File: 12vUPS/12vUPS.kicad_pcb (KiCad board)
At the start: 2 copper layers, 65.4 x 60.8 mm, 18 parts, among them J1 INPUT, J2 BATTERY, J3 OUTPUT, J4 ENABLE, K1 VEGHA L08A0212VDC, Q1 BDX53C

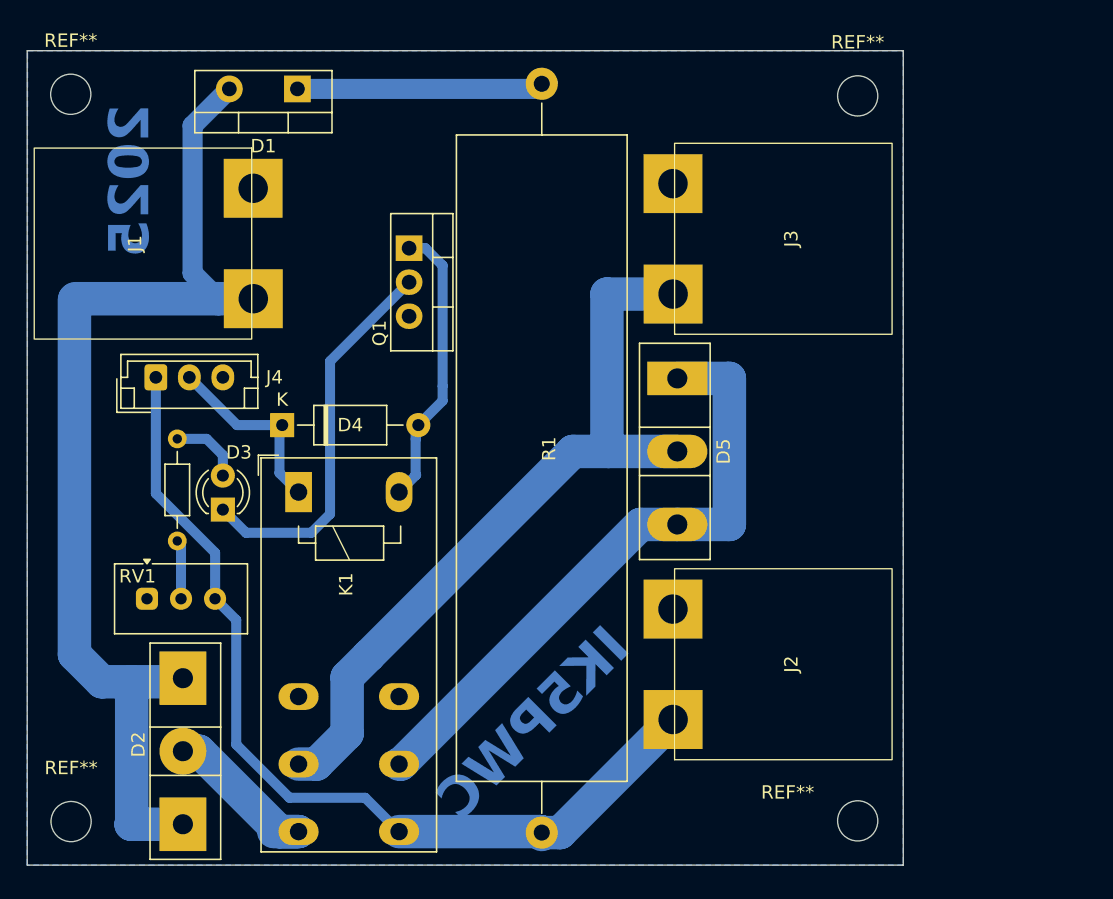
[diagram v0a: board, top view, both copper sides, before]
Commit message: Update 12vUPS-2025-06-08_110639.zip, 12vUPS-2025-06-08_231957.zip, 12vUPS-2025-06-08_232518.zip, and 11 more files
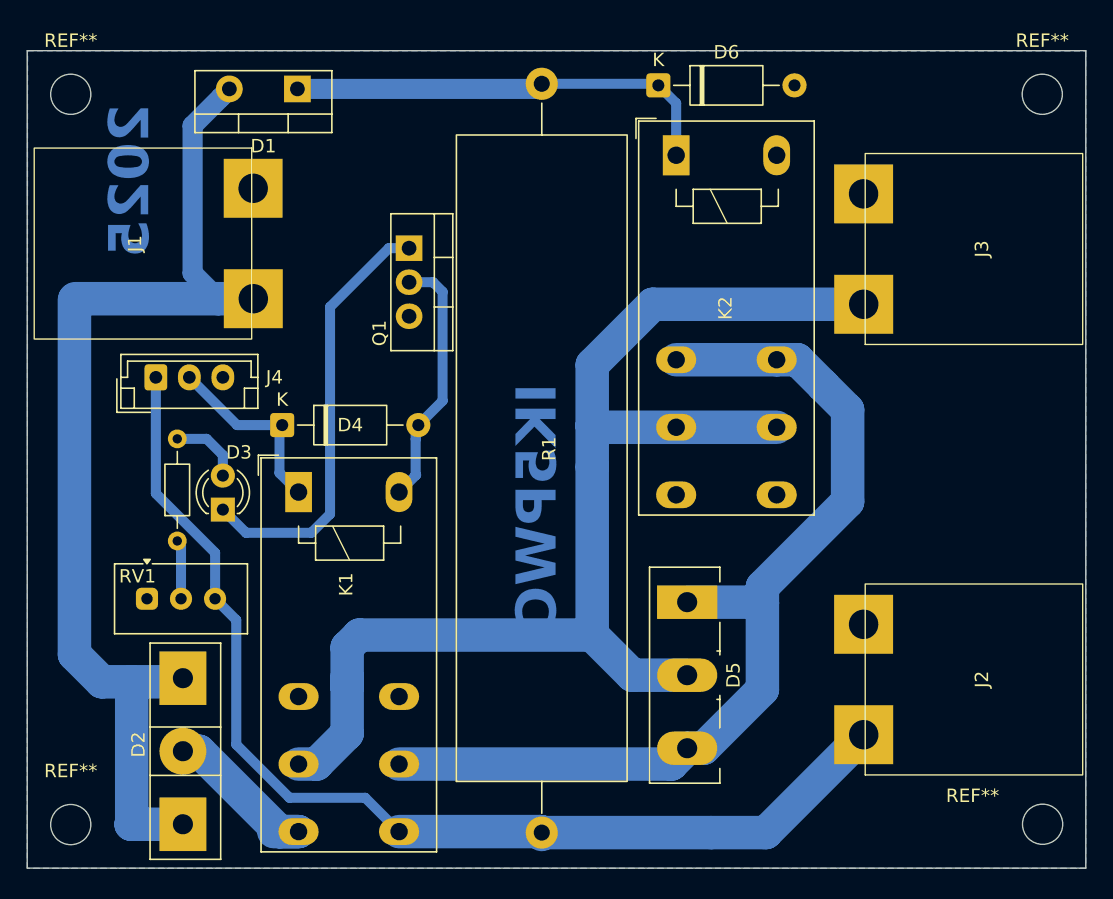
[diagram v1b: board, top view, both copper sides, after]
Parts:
- added D6: 1N4001, Diode_THT:D_A-405_P10.16mm_Horizontal, F.Cu at (59.9, 19.0)
- added K2: VEGHA L08A0212VDC, IK5PWC:VEGhA L08 12V dc, F.Cu at (61.2, 24.2)
- moved D5 16.7 mm to (62.0, 57.5)
- moved J2 14.3 mm to (75.2, 67.4)
- moved J3 14.2 mm to (75.2, 35.3)
- moved REF** 13.8 mm to (88.6, 74.1)
- moved REF** 13.8 mm to (88.5, 19.6)
- moved REF** 0.23 mm to (16.0, 74.1)
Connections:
- net /A1 renamed /ENA
- net Net-(D1-K) renamed /X1
- D4 pad 2: /A2 -> Net-(D4-A)
- K1 pad A2: /A2 -> Net-(D4-A)
- Q1 pad 1: /A2 -> Net-(D3-K)
- Q1 pad 2: Net-(D3-K) -> Net-(D4-A)
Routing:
- net Net-(D5-K): track 57.1 -> 94.8 mm
- net Net-(D5-A-Pad1): track 46.8 -> 72.9 mm
- net /A2: track 21.5 -> 0.00 mm
- net Net-(D4-A): track 0.00 -> 19.3 mm
- net /X1: track 19.1 -> 33.6 mm
- net /+12V: track 69.0 -> 82.8 mm
- net Net-(D3-K): track 29.0 -> 32.5 mm
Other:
- board size 65.4 x 60.8 mm -> 79 x 61 mm

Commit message: Update 12vUPS-2025-06-10_185612.zip, 12vUPS-2025-06-10_190121.zip, 12vUPS-2025-06-10_190645.zip, and 3 more files
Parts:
- removed D5: D_Schottky_Dual_CommonCathode_AKA_Parallel, Package_TO_SOT_THT:TO-247-3_Vertical
- removed K2: VEGHA L08A0212VDC, IK5PWC:VEGhA L08 12V dc
- D6: value 1N4001 -> W01G; footprint Diode_THT:D_A-405_P10.16mm_Horizontal -> Diode_THT:Diode_Bridge_Round_D9.8mm
- moved D6 24.9 mm to (35.5, 24.3)
- moved R2 7.55 mm to (24.0, 45.4), turned to -90 degrees
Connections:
- D1 pad 1: /X1 -> Net-(D1-K)
- D1 pad 2: VCC -> /INPUT
- D2 pad 2: VCC -> /INPUT
- D6 pad 1: /X1 -> Net-(D6-+)
- D6 pad 2: GND -> /OUT
- J1 pad 2: VCC -> /INPUT
- J2 pad 1: /+12V -> /BATT
- J3 pad 1: Net-(D5-K) -> /OUT
- J4 pad 1: /+12V -> /BATT
- K1 pad 11: Net-(D5-K) -> /OUT
- K1 pad 24: /+12V -> /BATT
- R1 pad 1: /+12V -> /BATT
- R1 pad 2: /X1 -> Net-(D1-K)
- R2 pad 1: Net-(R2-Pad1) -> Net-(D3-A)
- R2 pad 2: Net-(D3-A) -> Net-(R2-Pad2)
- RV1 pad 2: Net-(R2-Pad1) -> Net-(R2-Pad2)
- RV1 pad 3: /+12V -> Net-(D6-+)
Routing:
- net Net-(D5-K): track 94.8 -> 0.00 mm
- net /OUT: track 0.00 -> 85.1 mm
- net /+12V: track 82.8 -> 0.00 mm
- net VCC: track 78.2 -> 0.00 mm
- net /INPUT: track 0.00 -> 78.2 mm
- net Net-(D7-A): track 72.9 -> 0.00 mm
- net /BATT: track 0.00 -> 60.5 mm
- net /X1: track 33.6 -> 0.00 mm
- net Net-(D2-K): track 13.0 -> 45.5 mm
- net Net-(D1-K): track 0.00 -> 19.1 mm
- net Net-(R2-Pad2): track 0.00 -> 4.43 mm
- net Net-(R2-Pad1): track 4.43 -> 0.00 mm

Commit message: Update #auto_saved_files#, 12vUPS-2025-06-02_175555.zip, 12vUPS-2025-06-02_180136.zip, and 18 more files
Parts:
- removed D2: 30CPF04, IK5PWC:30CPF04
- removed D6: W01G, Diode_THT:Diode_Bridge_Round_D9.8mm
- added D7: D_Ideal, IK5PWC:D_IDEAL_with_GND, F.Cu at (76.3, 58.9)
- D1: value BYW19 -> SF30GG; footprint Package_TO_SOT_THT:TO-220-2_Vertical -> Diode_THT:D_DO-201AD_P15.24mm_Horizontal
- D3: value LED_Small -> 60CPQ150; footprint LED_THT:LED_D3.0mm -> Package_TO_SOT_THT:TO-247-3_Vertical
- moved D1 29.1 mm to (62.1, 20.0), turned to -90 degrees
- moved D3 23.6 mm to (25.0, 74.1)
- moved REF** 20.1 mm to (68.4, 74.1)
- moved REF** 20.1 mm to (68.4, 19.6)
- moved R2 8.08 mm to (28.3, 52.3), turned to 180 degrees
- moved J2 6.59 mm to (75.1, 74.0)
- moved J4 2.76 mm to (21.5, 43.4)
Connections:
- D1 pad 2: /INPUT -> /OUT
- D3 pad 1: Net-(D3-K) -> /DC_IN
- D3 pad 2: Net-(D3-A) -> /DC-IN-RELE
- D4 pad 2: Net-(D4-A) -> /BJT-GND
- J1 pad 2: /INPUT -> /DC_IN
- J2 pad 1: /BATT -> /BATT_IN
- J4 pad 1: /BATT -> /DC-IN-RELE
- J4 pad 3: GND -> /BJT-GND
- K1 pad 14: Net-(D2-K) -> /DC-IN-RELE
- K1 pad 21: Net-(D7-A) -> /OUT
- K1 pad 24: /BATT -> /DC-IN-RELE
- K1 pad A2: Net-(D4-A) -> /BJT-GND
- Q1 pad 1: Net-(D3-K) -> Net-(Q1-B)
- Q1 pad 2: Net-(D4-A) -> /BJT-GND
- R1 pad 1: /BATT -> /BATT_IN
- R2 pad 1: Net-(D3-A) -> Net-(Q1-B)
- RV1 pad 3: Net-(D6-+) -> /DC-IN-RELE
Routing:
- net /DC-IN-RELE: track 0.00 -> 80.4 mm
- net /INPUT: track 78.2 -> 0.00 mm
- net /BATT_IN: track 0.00 -> 62.0 mm
- net /DC_IN: track 0.00 -> 61.8 mm
- net /BATT: track 60.5 -> 0.00 mm
- net Net-(D2-K): track 45.5 -> 0.00 mm
- net Net-(Q1-B): track 0.00 -> 37.7 mm
- net /BJT-GND: track 0.00 -> 37.5 mm
- net Net-(D3-K): track 32.5 -> 0.00 mm
- net Net-(D4-A): track 19.3 -> 0.00 mm
- net /OUT: track 85.1 -> 67.6 mm
- net Net-(D1-K): track 19.1 -> 12.2 mm
- net Net-(D3-A): track 5.43 -> 0.00 mm
- net Net-(R2-Pad2): track 4.43 -> 5.75 mm
- net /ENA: track 14.0 -> 14.5 mm

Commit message: Update 12vUPS-2025-06-06_224542.zip, 12vUPS-2025-06-06_225111.zip, 12vUPS-2025-06-06_225614.zip, and 28 more files
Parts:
- removed R2: 510, Resistor_THT:R_Axial_DIN0204_L3.6mm_D1.6mm_P7.62mm_Horizontal
- added D5: D, Diode_THT:D_DO-41_SOD81_P10.16mm_Horizontal, F.Cu at (18.2, 59.9)
- added D6: 4V1, Diode_THT:D_DO-35_SOD27_P7.62mm_Horizontal, F.Cu at (20.7, 50.2)
- J4: footprint Connector_JST:JST_EH_B3B-EH-A_1x03_P2.50mm_Vertical -> Connector_JST:JST_EH_B4B-EH-A_1x04_P2.50mm_Vertical
- Q1: value BDX53C -> BC337; footprint Package_TO_SOT_THT:TO-220-3_Vertical -> Package_TO_SOT_THT:TO-92_Inline_Wide
- moved Q1 7.84 mm to (41.9, 38.9), turned to 90 degrees
- moved D3 6.76 mm to (26.7, 67.5), turned to 180 degrees
- moved D4 4.58 mm to (36.4, 44.6), turned to 90 degrees
- moved RV1 2.47 mm to (21.8, 54.8)
- moved J4 2.23 mm to (23.2, 41.9)
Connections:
- D7 pad 1: /DC-IN-RELE -> Net-(D7-K)
- J4 pad 2: /ENA -> Net-(D7-K)
- J4 pad 3: /BJT-GND -> /ENA
- K1 pad 24: /DC-IN-RELE -> Net-(D7-K)
- Q1 pad 1: Net-(Q1-B) -> /BJT-GND
- Q1 pad 2: /BJT-GND -> Net-(D6-A)
- RV1 pad 3: /DC-IN-RELE -> Net-(D5-K)
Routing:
- net Net-(D7-K): track 0.00 -> 72.7 mm
- net Net-(Q1-B): track 37.7 -> 0.00 mm
- net Net-(D6-A): track 0.00 -> 33.1 mm
- net /DC-IN-RELE: track 80.4 -> 52.7 mm
- net Net-(D5-K): track 0.00 -> 12.0 mm
- net /BATT_IN: track 62.0 -> 53.8 mm
- net /BJT-GND: track 37.5 -> 29.8 mm
- net /DC_IN: track 61.8 -> 59.8 mm
- net /ENA: track 14.5 -> 16.5 mm
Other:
- board text added: "DC UPS"

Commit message: Update 12vUPS-2025-06-08_233608.zip, 12vUPS-2025-06-08_234122.zip, 12vUPS-2025-06-22_122202.zip, and 5 more files
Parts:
- D7: footprint IK5PWC:D_IDEAL_with_GND -> IK5PWC:D_IDEAL_no_GND
- moved D7 11.4 mm to (70.2, 49.3), turned to 0 degrees
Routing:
- net Net-(D7-K): track 72.7 -> 79.1 mm
- net /BATT_IN: track 53.8 -> 58.3 mm
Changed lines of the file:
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@@
 		)
 	)
-	(footprint "IK5PWC:D_IDEAL_with_GND"
+	(footprint "IK5PWC:D_IDEAL_no_GND"
 		(layer "F.Cu")
-		(at 76.2975 58.9325 180)
+		(at 70.2175 49.2525)
 		(descr "terminal block Metz Connect Type703_RT10N02HGLU, 2 pins, pitch 9.52mm, size 19x12.5mm^2, drill diamater 1.3mm, pad diameter 2.6mm, see http://www.metz-connect.com/de/system/files/productfiles/Datenblatt_317031_RT10NxxHGLU_OFF-022897S.pdf, script-generated using https://github.com/pointhi/kicad-footprint-generator/scripts/TerminalBlock_MetzConnect")
 		(tags "THT terminal block Metz Connect Type703_RT10N02HGLU pitch 9.52mm size 19x12.5mm^2 drill 1.3mm pad 2.6mm")
@@
 		)
 		(property "Value" "D_Ideal"
-			(at 5.3 -0.23 0)
+			(at -1.4775 -1.935 0)
 			(layer "F.Fab")
 			(effects
@@
 		)
 		(property "Datasheet" ""
-			(at 4.32 25.08 180)
+			(at 4.32 25.08 0)
 			(unlocked yes)
 			(layer "F.Fab")
@@
 		)
 		(property "Description" "Diode"
-			(at 4.32 25.08 180)
+			(at 4.32 25.08 0)
 			(unlocked yes)
 			(layer "F.Fab")
@@
 		)
 		(property "Sim.Device" "D"
-			(at 0 0 180)
+			(at 0 0 0)
 			(unlocked yes)
 			(layer "F.Fab")
@@
 		)
 		(property "Sim.Pins" "1=K 2=A 3=GND"
-			(at 0 0 180)
+			(at 0 0 0)
 			(unlocked yes)
 			(layer "F.Fab")
@@
 		(attr through_hole)
 		(fp_line
-			(start 6.26 -0.615)
-			(end 6.26 9.275)
-			(stroke
-				(width 0.5)
-				(type solid)
-			)
-			(layer "F.SilkS")
-		)
-		(fp_line
-			(start 1.315 4.33)
-			(end 11.205 4.33)
+			(start -3.91 1.77)
+			(end 1.06 1.77)
 			(stroke
 				(width 0.5)
@@
 		)
 		(fp_line
-			(start 1 4.33)
-			(end 5.97 4.33)
-			(stroke
-				(width 0.1)
-				(type default)
-			)
-			(layer "F.SilkS")
-		)
-		(fp_line
-			(start -2.595 4.33)
-			(end 7.295 4.33)
+			(start -0.195 -0.18)
+			(end -0.18 3.83)
 			(stroke
 				(width 0.5)
@@
 		)
 		(fp_rect
-			(start -9.87 11.75)
-			(end 18.12 19.65)
-			(stroke
-				(width 0.1)
-				(type default)
-			)
-			(fill no)
-			(layer "F.SilkS")
-		)
-		(fp_rect
-			(start -9.88 -3.15)
-			(end 18.12 19.65)
-			(stroke
-				(width 0.1)
-				(type solid)
-			)
-			(fill no)
-			(layer "F.SilkS")
-		)
-		(fp_rect
 			(start -9.88 -3.15)
-			(end 18.11 10.79)
+			(end 7.12 6.85)
 			(stroke
 				(width 0.1)
@@
 		(fp_poly
 			(pts
-				(xy 1 -0.615) (xy 1 9.275) (xy 1.025 9.275) (xy 5.97 4.33) (xy 1.025 -0.615)
+				(xy -2.68 -0.225) (xy -2.68 3.855) (xy -0.195 1.77)
 			)
 			(stroke
@@
 		(fp_rect
 			(start -9.98 -3.25)
-			(end 18.22 19.75)
+			(end 7.22 6.95)
 			(stroke
 				(width 0.1)
@@
 			(layer "F.CrtYd")
 		)
-		(fp_line
-			(start 18.11 17.65)
-			(end -9.88 17.65)
-			(stroke
-				(width 0.1)
-				(type solid)
-			)
-			(layer "User.9")
-		)
 		(fp_text user "${REFERENCE}"
-			(at 4.13 17.46 0)
+			(at -0.95 8.42 0)
 			(layer "F.Fab")
 			(effects
@@
 			)
 		)
-		(pad "1" thru_hole circle
-			(at 14.34 4.3 180)
-			(size 5.5 5.5)
-			(drill 2.3)
+		(pad "1" thru_hole rect
+			(at -8.07 5.05)
+			(size 3.5 3.5)
+			(drill 2)
 			(layers "*.Cu" "*.Mask")
 			(remove_unused_layers no)
@@
 			(pintype "passive")
 		)
-		(pad "2" thru_hole circle
-			(at -6.2 4.3 180)
-			(size 5.5 5.5)
-			(drill 2.3)
+		(pad "1" thru_hole rect
+			(at -8.06 -1.34)
+			(size 3.5 3.5)
+			(drill 2)
 			(layers "*.Cu" "*.Mask")
 			(remove_unused_layers no)
-			(net 9 "/BATT_IN")
-			(pinfunction "A")
+			(net 11 "Net-(D7-K)")
+			(pinfunction "K")
 			(pintype "passive")
 		)
-		(pad "3" thru_hole circle
-			(at -6.2 15.01 180)
-			(size 5.5 5.5)
-			(drill 2.3)
+		(pad "2" thru_hole rect
+			(at 5.3 5.04)
+			(size 3.5 3.5)
+			(drill 2)
 			(layers "*.Cu" "*.Mask")
 			(remove_unused_layers no)
-			(net 1 "GND")
-			(pinfunction "GND")
+			(net 9 "/BATT_IN")
+			(pinfunction "A")
 			(pintype "passive")
 		)
-		(pad "3" thru_hole circle
-			(at 14.3 15.01 180)
-			(size 5.5 5.5)
-			(drill 2.3)
+		(pad "2" thru_hole rect
+			(at 5.32 -1.35)
+			(size 3.5 3.5)
+			(drill 2)
 			(layers "*.Cu" "*.Mask")
 			(remove_unused_layers no)
-			(net 1 "GND")
-			(pinfunction "GND")
+			(net 9 "/BATT_IN")
+			(pinfunction "A")
 			(pintype "passive")
 		)
 		(group ""
-			(members "1e930a74-decf-4d0d-b22a-d9020ec64da4" "38462f81-1908-4855-8697-cc14553c1441"
-				"4fe994f1-ae68-4926-844e-d0983c92209b" "89733ad4-0324-4e29-9c96-dd42813075d6"
-				"be10e844-67ce-4d0a-9af0-51a7b58a24ff"
+			(members "01b3dc8c-98e9-4f63-9327-647c1e07778b" "70d5449d-6eb7-4598-9863-d922e2f8df2a"
+				"a28f07d8-7345-473e-b98f-a46c4aaf5118"
 			)
 		)
@@
 	)
 	(segment
-		(start 67.1375 64.7575)
-		(end 70.381 61.514)
+		(start 75.5375 54.3125)
+		(end 75.5375 47.9125)
 		(width 2.5)
 		(layer "B.Cu")
@@
 	)
 	(segment
-		(start 67.1375 69.306)
-		(end 67.1375 64.7575)
+		(start 75.5375 47.9125)
+		(end 75.5475 47.9025)
 		(width 2.5)
 		(layer "B.Cu")
@@
 	)
 	(segment
-		(start 70.381 61.514)
-		(end 77.2625 54.6325)
-		(width 2.5)
-		(layer "B.Cu")
-		(net 9)
-	)
-	(segment
 		(start 50.9725 74.6625)
 		(end 51.1875 74.8775)
@@
 	)
 	(segment
-		(start 77.2625 54.6325)
-		(end 82.4975 54.6325)
+		(start 75.0975 74.0225)
+		(end 70.381 69.306)
 		(width 2.5)
 		(layer "B.Cu")
@@
 	)
 	(segment
-		(start 75.0975 74.0225)
-		(end 70.381 69.306)
+		(start 75.5375 54.3125)
+		(end 69.1575 54.3125)
 		(width 2.5)
 		(layer "B.Cu")
@@
 	)
 	(segment
+		(start 67.1375 56.3325)
+		(end 67.1375 69.306)
+		(width 2.5)
+		(layer "B.Cu")
+		(net 9)
+	)
+	(segment
 		(start 70.381 69.306)
 		(end 67.1375 69.306)
@@
 	)
 	(segment
+		(start 69.1575 54.3125)
+		(end 67.1375 56.3325)
+		(width 2.5)
+		(layer "B.Cu")
+		(net 9)
+	)
+	(segment
 		(start 74.3842 74.7358)
 		(end 75.0975 74.0225)
@@
 	)
 	(segment
+		(start 62.1475 54.3125)
+		(end 62.1475 47.9125)
+		(width 2.5)
+		(layer "B.Cu")
+		(net 11)
+	)
+	(segment
 		(start 30.1375 71.0925)
 		(end 31.5475 72.5025)
@@
 	)
 	(segment
+		(start 62.1475 47.9125)
+		(end 62.1575 47.9025)
+		(width 2.5)
+		(layer "B.Cu")
+		(net 11)
+	)
+	(segment
 		(start 23.9275 59.9025)
 		(end 26.8875 56.9425)
@@
 		(filled_areas_thickness no)
 		(keepout
-			(tracks not_allowed)
-			(vias not_allowed)
-			(pads not_allowed)
+			(tracks allowed)
+			(vias allowed)
+			(pads allowed)
 			(copperpour not_allowed)
 			(footprints allowed)
@@
 		(polygon
 			(pts
-				(xy 57.1875 50.9375) (xy 82.7375 50.9625) (xy 76.8875 52.3625)
+				(xy 56.9675 47.0525) (xy 66.8775 53.8625) (xy 72.9975 46.0325)
 			)
 		)

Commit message: Update .~lock.12vUPS.csv#, 12vUPS-2025-06-10_185612.zip, 12vUPS-2025-06-10_190121.zip, and 11 more files
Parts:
- moved D7 4.58 mm to (67.4, 52.9), turned to 180 degrees
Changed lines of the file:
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@@
 	(footprint "IK5PWC:D_IDEAL_no_GND"
 		(layer "F.Cu")
-		(at 70.2175 49.2525)
-		(descr "terminal block Metz Connect Type703_RT10N02HGLU, 2 pins, pitch 9.52mm, size 19x12.5mm^2, drill diamater 1.3mm, pad diameter 2.6mm, see http://www.metz-connect.com/de/system/files/productfiles/Datenblatt_317031_RT10NxxHGLU_OFF-022897S.pdf, script-generated using https://github.com/pointhi/kicad-footprint-generator/scripts/TerminalBlock_MetzConnect")
-		(tags "THT terminal block Metz Connect Type703_RT10N02HGLU pitch 9.52mm size 19x12.5mm^2 drill 1.3mm pad 2.6mm")
+		(at 67.4375 52.8925 180)
 		(property "Reference" "D7"
 			(at 9.5 6.95 0)
@@
 		)
 		(property "Datasheet" ""
-			(at 4.32 25.08 0)
+			(at 4.32 25.08 180)
 			(unlocked yes)
 			(layer "F.Fab")
@@
 		)
 		(property "Description" "Diode"
-			(at 4.32 25.08 0)
+			(at 4.32 25.08 180)
 			(unlocked yes)
 			(layer "F.Fab")
@@
 		)
 		(property "Sim.Device" "D"
-			(at 0 0 0)
+			(at 0 0 180)
 			(unlocked yes)
 			(layer "F.Fab")
@@
 		)
 		(property "Sim.Pins" "1=K 2=A 3=GND"
-			(at 0 0 0)
+			(at 0 0 180)
 			(unlocked yes)
 			(layer "F.Fab")
@@
 		(attr through_hole)
 		(fp_line
-			(start -3.91 1.77)
-			(end 1.06 1.77)
+			(start -0.195 -0.18)
+			(end -0.18 3.83)
 			(stroke
 				(width 0.5)
@@
 		)
 		(fp_line
-			(start -0.195 -0.18)
-			(end -0.18 3.83)
+			(start -3.91 1.77)
+			(end 1.06 1.77)
 			(stroke
 				(width 0.5)
@@
 		)
 		(pad "1" thru_hole rect
-			(at -8.07 5.05)
+			(at 5.3 5.04 180)
 			(size 3.5 3.5)
 			(drill 2)
@@
 		)
 		(pad "1" thru_hole rect
-			(at -8.06 -1.34)
+			(at 5.32 -1.35 180)
 			(size 3.5 3.5)
 			(drill 2)
@@
 		)
 		(pad "2" thru_hole rect
-			(at 5.3 5.04)
+			(at -8.07 5.05 180)
 			(size 3.5 3.5)
 			(drill 2)
@@
 		)
 		(pad "2" thru_hole rect
-			(at 5.32 -1.35)
+			(at -8.06 -1.34 180)
 			(size 3.5 3.5)
 			(drill 2)
@@
 		)
 		(group ""
-			(members "01b3dc8c-98e9-4f63-9327-647c1e07778b" "70d5449d-6eb7-4598-9863-d922e2f8df2a"
-				"a28f07d8-7345-473e-b98f-a46c4aaf5118"
+			(members "5fed0ce8-7779-4a95-b375-404f8e024d4d" "91d9a5bc-cb86-4936-8ba5-b8df524cc810"
+				"c459324a-e02f-4efd-9290-394ebb01aea0"
 			)
 		)
